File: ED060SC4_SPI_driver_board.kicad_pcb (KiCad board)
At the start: 4 copper layers, 71.2 x 44.5 mm, 83 parts, among them J1 ED060SC4, J2 Conn_01x06, J3 Conn_01x04, J4 Conn_01x04, J5 Conn_01x06, J6 Conn_01x02, SW1 SS12D07VG2, SW2 DSIC01LSGET, U1 TPS65185RGZR, U2 STM32F103C8T6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

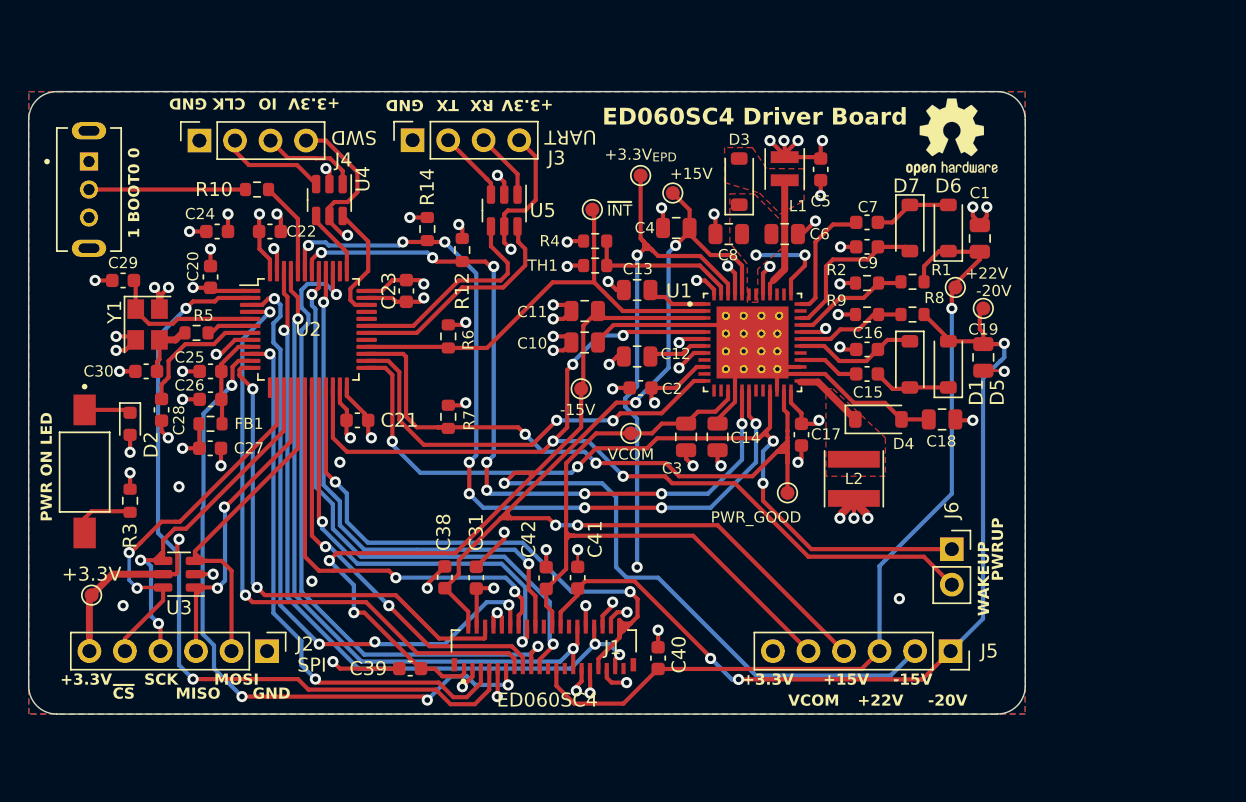
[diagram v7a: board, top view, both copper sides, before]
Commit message: Add mounting holes
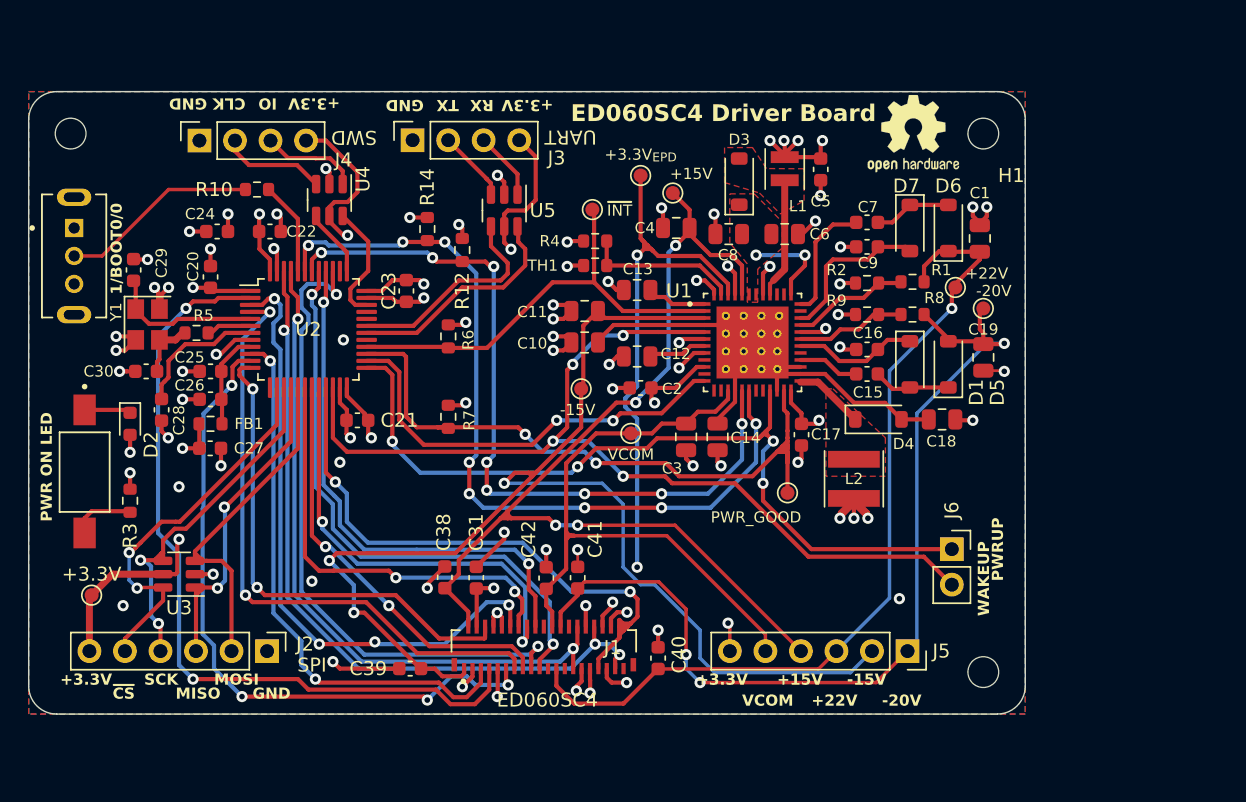
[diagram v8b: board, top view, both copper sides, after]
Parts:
- added H1: M3 hole, MountingHole:MountingHole_2.2mm_M2, F.Cu at (116.2, 54.5)
- added H2: M3 hole, MountingHole:MountingHole_2.2mm_M2, F.Cu at (116.2, 93.0)
- added H4: M3 hole, MountingHole:MountingHole_2.2mm_M2, F.Cu at (51.0, 54.5)
- moved SW1 4.87 mm to (51.2, 63.2)
- moved J5 3.08 mm to (110.8, 91.5)
- moved REF** 2.76 mm to (111.2, 54.5)
- moved C29 1.06 mm to (55.5, 64.2), turned to -90 degrees
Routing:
- net +15V: track 76.8 -> 73.7 mm
- net /SW_BOOT0: track 11.2 -> 14.2 mm
- net -15V: track 95.0 -> 92.7 mm
- net VCOM: track 48.4 -> 46.0 mm
- net +3.3V_{EPD}: track 51.9 -> 53.9 mm, vias 8 -> 9
- net +22V: track 63.5 -> 61.7 mm
- net -20V: track 66.9 -> 68.4 mm
- net GND: vias 68 -> 69
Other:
- board text added: "1/BOOT0/0"
- board text removed: "1 BOOT0 0"
